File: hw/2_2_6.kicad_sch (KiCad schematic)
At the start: 2 parts

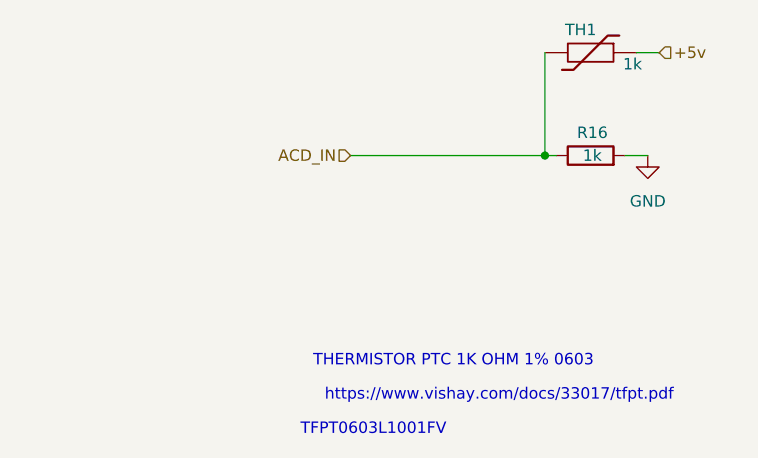
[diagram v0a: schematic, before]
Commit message: Add LM2576S-5 to 2.3.10
Signed-off-by: ckalina <46683072+ckalina@users.noreply.github.com>
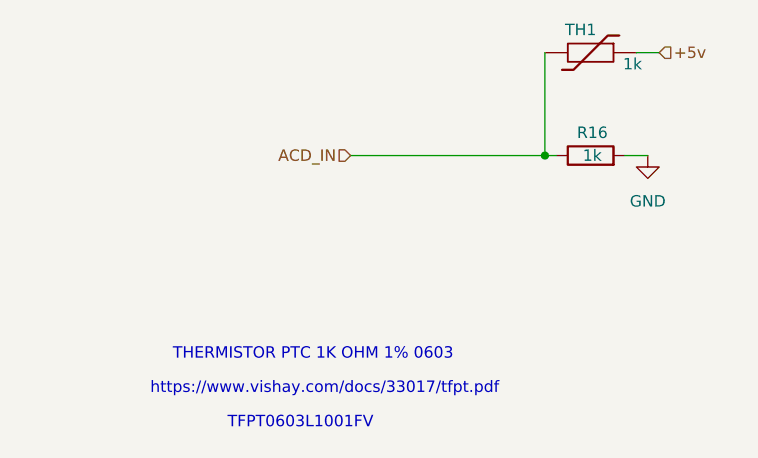
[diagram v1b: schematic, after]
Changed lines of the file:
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@@
   )
   (text "TFPT0603L1001FV" (at 129.54 121.92 180)
-    (effects (font (size 1.27 1.27)))
+    (effects (font (size 1.27 1.27)) (justify right bottom))
   )
   (text "THERMISTOR PTC 1K OHM 1% 0603 " (at 138.43 114.3 180)
-    (effects (font (size 1.27 1.27)))
+    (effects (font (size 1.27 1.27)) (justify right bottom))
   )
   (text "https://www.vishay.com/docs/33017/tfpt.pdf" (at 143.51 118.11 180)
-    (effects (font (size 1.27 1.27)))
+    (effects (font (size 1.27 1.27)) (justify right bottom))
   )
   (hierarchical_label "ACD_IN" (shape input) (at 127 91.44 180)
